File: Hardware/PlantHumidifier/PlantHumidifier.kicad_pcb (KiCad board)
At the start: 2 copper layers, 10 parts, among them J1 110990030, J2 Conn_01x05_Female, J3 Conn_01x04_Female, J4 Conn_01x04_Female, SW1 SW_SPST, U1 WeMos_D1_mini

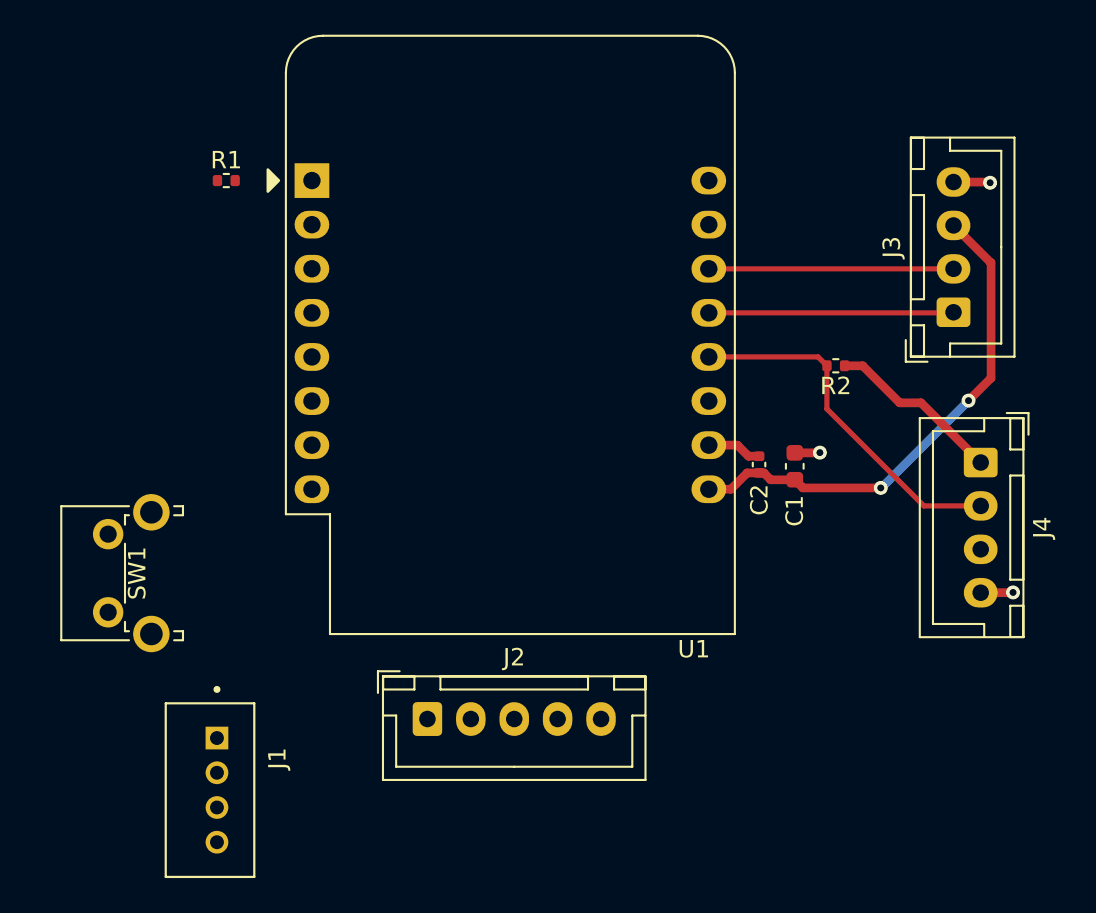
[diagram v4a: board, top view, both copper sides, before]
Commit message: Layout: Reflect new pin changes
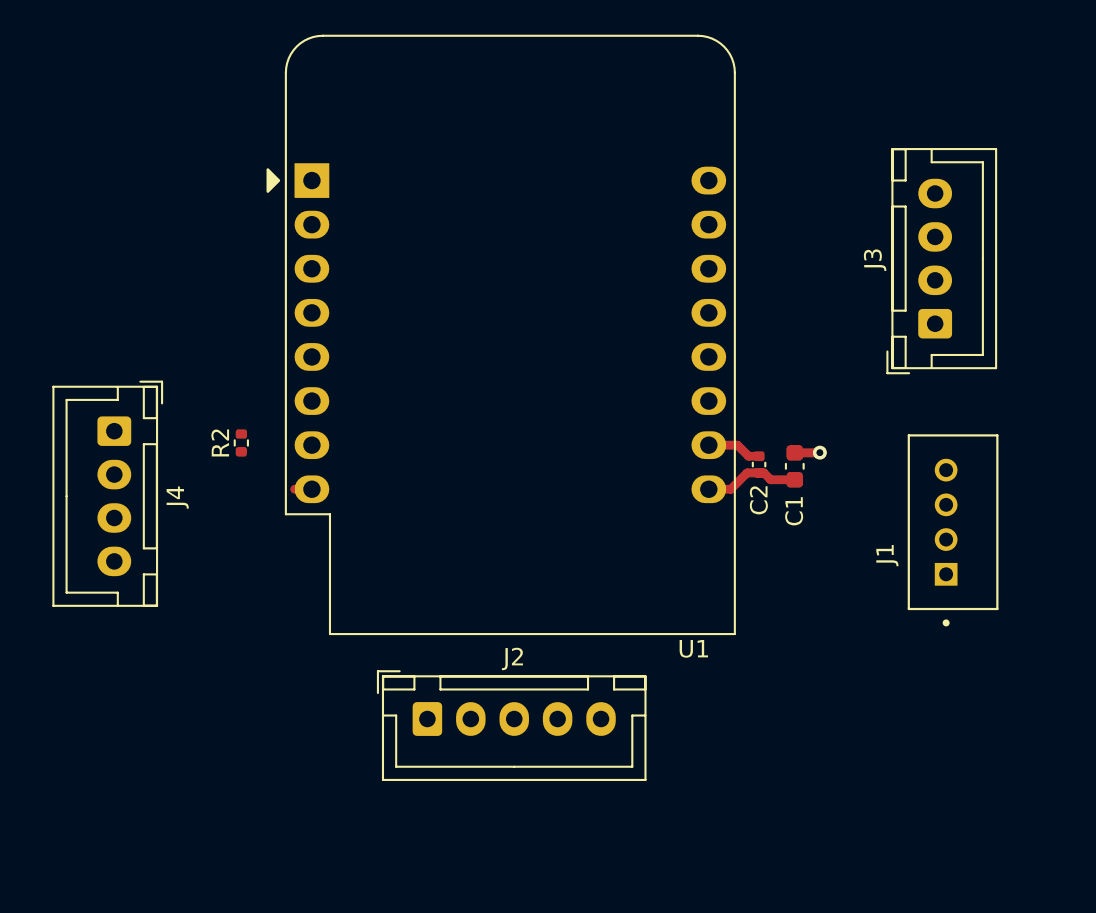
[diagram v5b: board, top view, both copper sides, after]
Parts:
- removed R1: 10k, Resistor_SMD:R_0402_1005Metric
- removed SW1: SW_SPST, Button_Switch_THT:SW_Tactile_SPST_Angled_PTS645Vx83-2LFS
- moved J4 49.9 mm to (66.2, 90.0)
- moved J1 44.7 mm to (114.1, 95.2), turned to 90 degrees
- moved R2 34.5 mm to (73.5, 90.7), turned to 90 degrees
- moved J3 1.25 mm to (113.5, 83.8)
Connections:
- J2 pad 3: /Encoder_SW -> /Rst_n
- J4 pad 1: +3V3 -> /DHT22_Sense
- J4 pad 2: /DHT22_Sense -> +3V3
- U1 pad 12: /DHT22_Sense -> unconnected-(U1-Pad12)
- U1 pad 3: /Encoder_SW -> /Atomizer
- U1 pad 6: unconnected-(U1-Pad6) -> /DHT22_Sense
- U1 pad 7: /Atomizer -> unconnected-(U1-Pad7)
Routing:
- net +5V: track 29.3 -> 5.51 mm, vias 2 -> 0
- net /DHT22_Sense: track 20.7 -> 0.00 mm
- net /OLED_SDA: track 14.1 -> 0.00 mm
- net /OLED_SCL: track 14.1 -> 0.00 mm
- net +3V3: track 10.1 -> 0.99 mm
- net GND: track 8.66 -> 4.66 mm, vias 3 -> 1

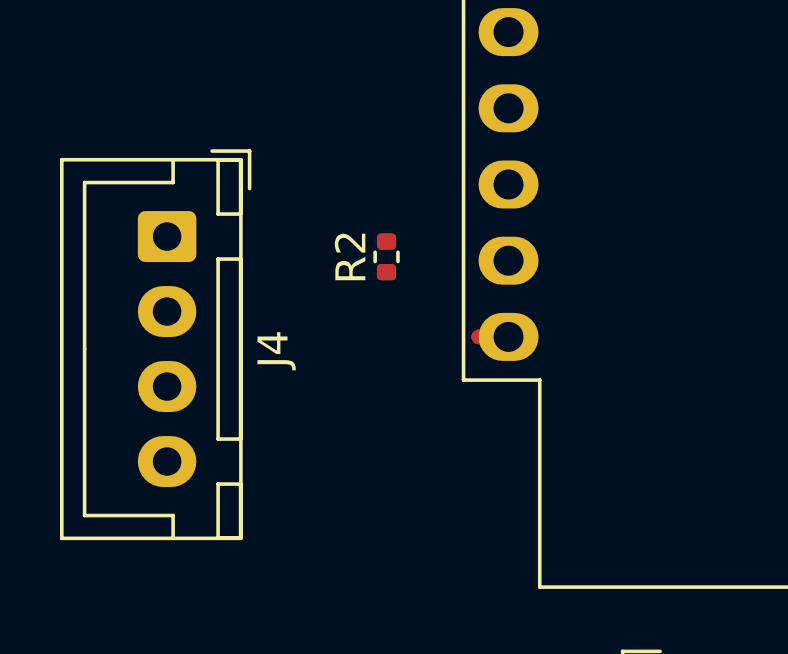
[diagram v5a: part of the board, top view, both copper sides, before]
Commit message: Layout: Route DHT22
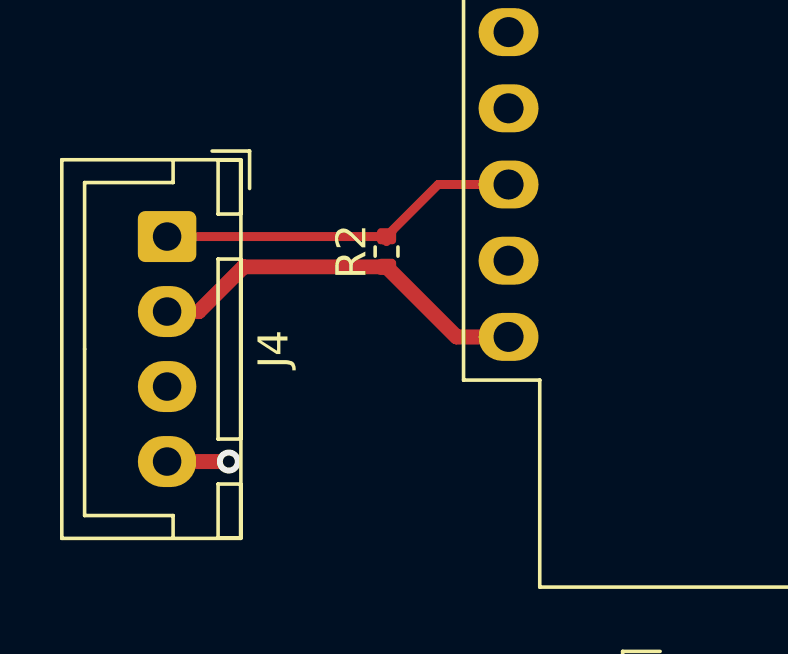
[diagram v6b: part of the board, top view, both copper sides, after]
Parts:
- moved R2 0.18 mm to (73.5, 90.5)
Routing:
- net /DHT22_Sense: track 0.00 -> 12.3 mm
- net +3V3: track 0.99 -> 13.0 mm
- net GND: track 4.66 -> 6.72 mm, vias 1 -> 2
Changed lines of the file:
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@@
   )
   (footprint "Resistor_SMD:R_0402_1005Metric" (layer "F.Cu")
-    (at 73.5076 90.678 90)
+    (at 73.5076 90.5 90)
     (descr "Resistor SMD 0402 (1005 Metric), square (rectangular) end terminal, IPC_7351 nominal, (Body size source: IPC-SM-782 page 72, https://www.pcb-3d.com/wordpress/wp-content/uploads/ipc-sm-782a_amendment_1_and_2.pdf), generated with kicad-footprint-generator")
     (tags "resistor")
@@
   (segment (start 101.7016 93.345) (end 102.644 92.4026) (width 0.5) (layer "F.Cu") (net 1))
   (segment (start 100.434 93.345) (end 101.7016 93.345) (width 0.5) (layer "F.Cu") (net 1))
+  (segment (start 66.1924 97.5) (end 68.25 97.5) (width 0.5) (layer "F.Cu") (net 2))
   (segment (start 106.82 91.2492) (end 106.8324 91.2368) (width 0.5) (layer "F.Cu") (net 2))
   (segment (start 105.3468 91.2114) (end 105.3846 91.2492) (width 0.5) (layer "F.Cu") (net 2))
@@
   (segment (start 102.0826 90.805) (end 102.7202 91.4426) (width 0.5) (layer "F.Cu") (net 2))
   (segment (start 102.7202 91.4426) (end 103.3272 91.4426) (width 0.5) (layer "F.Cu") (net 2))
+  (via (at 68.25 97.5) (size 0.8) (drill 0.4) (layers "F.Cu" "B.Cu") (net 2))
   (via (at 106.8324 91.2368) (size 0.8) (drill 0.4) (layers "F.Cu" "B.Cu") (net 2))
-  (segment (start 77.574 93.345) (end 76.581 93.345) (width 0.5) (layer "F.Cu") (net 10))
+  (segment (start 68.74 91.01) (end 73.5076 91.01) (width 0.5) (layer "F.Cu") (net 10))
+  (segment (start 73.5076 91.01) (end 75.8426 93.345) (width 0.5) (layer "F.Cu") (net 10))
+  (segment (start 75.8426 93.345) (end 77.574 93.345) (width 0.5) (layer "F.Cu") (net 10))
+  (segment (start 67.25 92.5) (end 68.74 91.01) (width 0.5) (layer "F.Cu") (net 10))
+  (segment (start 66.1924 92.5) (end 67.25 92.5) (width 0.5) (layer "F.Cu") (net 10))
+  (segment (start 73.4976 90) (end 73.5076 89.99) (width 0.3) (layer "F.Cu") (net 11))
+  (segment (start 73.5076 89.99) (end 75.2326 88.265) (width 0.3) (layer "F.Cu") (net 11))
+  (segment (start 75.2326 88.265) (end 77.574 88.265) (width 0.3) (layer "F.Cu") (net 11))
+  (segment (start 66.1924 90) (end 73.4976 90) (width 0.3) (layer "F.Cu") (net 11))
+  (segment (start 73.3396 90) (end 73.5076 90.168) (width 0.3) (layer "F.Cu") (net 11))
 )

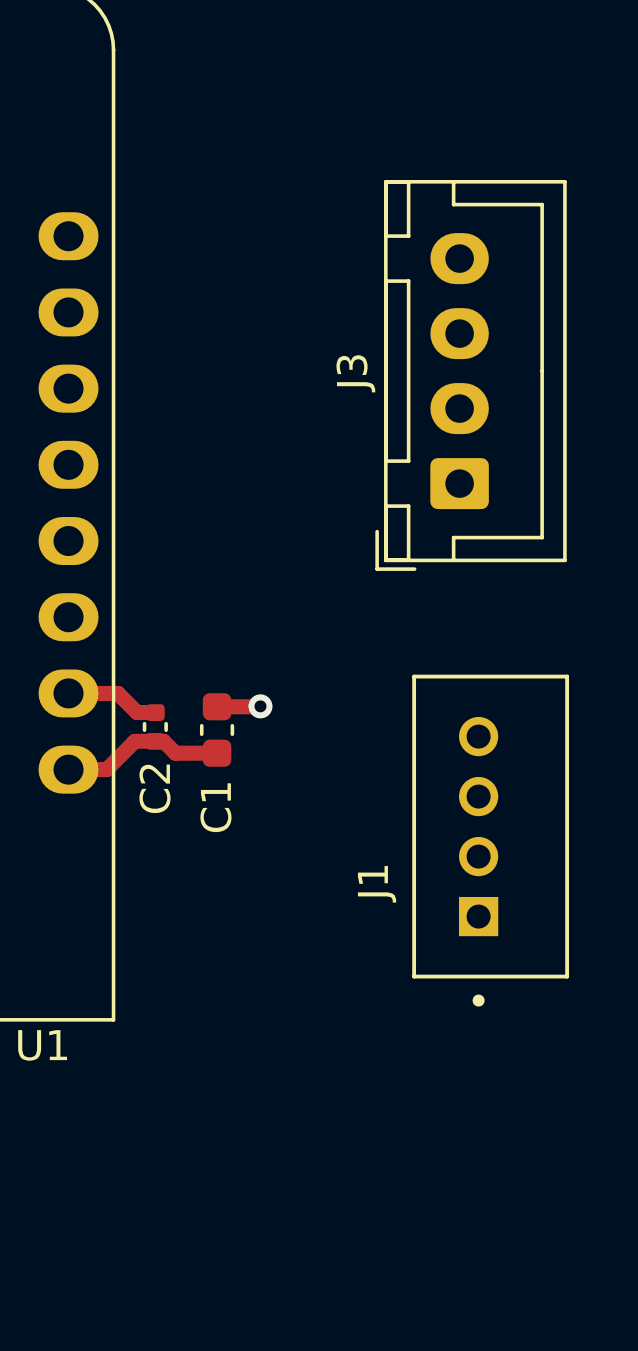
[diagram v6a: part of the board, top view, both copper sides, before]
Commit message: Change pin assignment for OLED for better routing
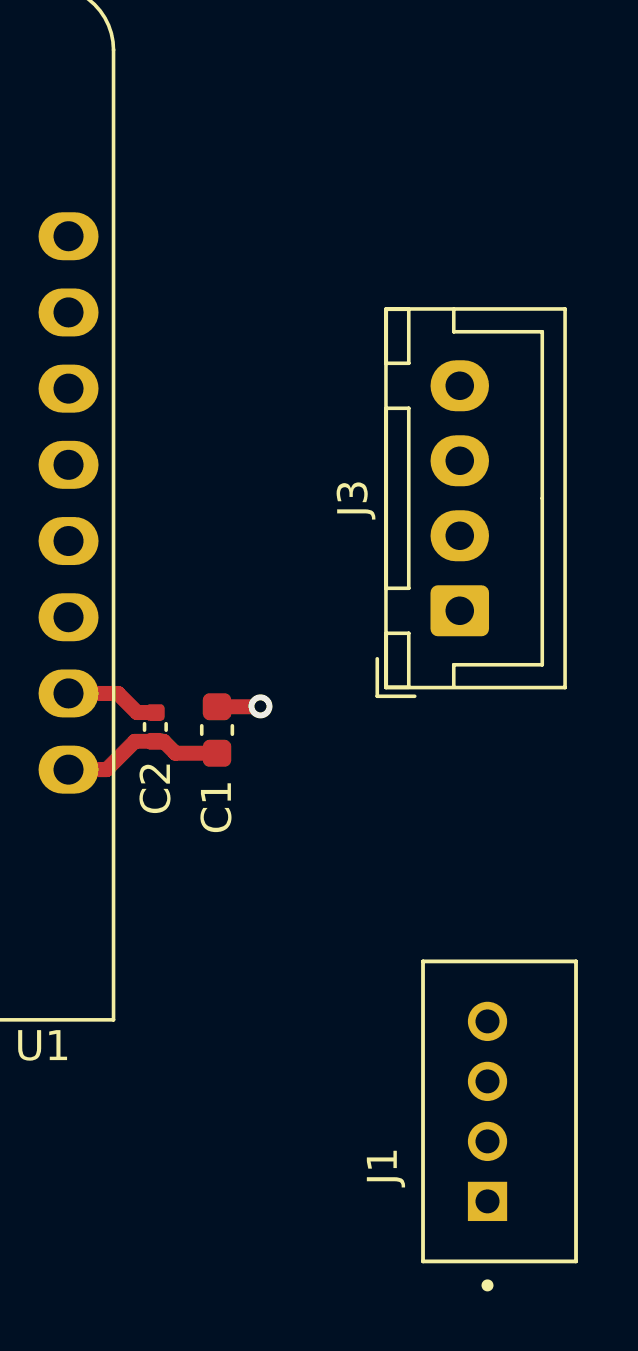
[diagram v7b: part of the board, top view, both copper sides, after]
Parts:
- moved J1 9.50 mm to (114.4, 104.7)
- moved J3 4.24 mm to (113.5, 88.0)
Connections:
- J3 pad 1: /OLED_SDA -> +5V
- J3 pad 2: /OLED_SCL -> GND
- J3 pad 3: +5V -> /OLED_SDA
- J3 pad 4: GND -> /OLED_SCL
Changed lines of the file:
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@@
   )
   (footprint "Connector_JST:JST_XH_B4B-XH-A_1x04_P2.50mm_Vertical" (layer "F.Cu")
-    (at 113.4702 83.8108 90)
+    (at 113.475 88.05 90)
     (descr "JST XH series connector, B4B-XH-A (http://www.jst-mfg.com/product/pdf/eng/eXH.pdf), generated with kicad-footprint-generator")
     (tags "connector JST XH vertical")
@@
     (fp_line (start -2.45 3.4) (end 9.95 3.4) (layer "F.Fab") (width 0.1))
     (pad "1" thru_hole roundrect (at 0 0 90) (size 1.7 1.95) (drill 0.95) (layers *.Cu *.Mask) (roundrect_rratio 0.147059)
-      (net 5 "/OLED_SDA") (pinfunction "Pin_1") (pintype "passive"))
+      (net 1 "+5V") (pinfunction "Pin_1") (pintype "passive"))
     (pad "2" thru_hole oval (at 2.5 0 90) (size 1.7 1.95) (drill 0.95) (layers *.Cu *.Mask)
-      (net 6 "/OLED_SCL") (pinfunction "Pin_2") (pintype "passive"))
+      (net 2 "GND") (pinfunction "Pin_2") (pintype "passive"))
     (pad "3" thru_hole oval (at 5 0 90) (size 1.7 1.95) (drill 0.95) (layers *.Cu *.Mask)
-      (net 1 "+5V") (pinfunction "Pin_3") (pintype "passive"))
+      (net 5 "/OLED_SDA") (pinfunction "Pin_3") (pintype "passive"))
     (pad "4" thru_hole oval (at 7.5 0 90) (size 1.7 1.95) (drill 0.95) (layers *.Cu *.Mask)
-      (net 2 "GND") (pinfunction "Pin_4") (pintype "passive"))
+      (net 6 "/OLED_SCL") (pinfunction "Pin_4") (pintype "passive"))
     (model "${KICAD6_3DMODEL_DIR}/Connector_JST.3dshapes/JST_XH_B4B-XH-A_1x04_P2.50mm_Vertical.wrl"
       (offset (xyz 0 0 0))
@@
   )
   (footprint "Seeed_Connectors:SEEED_110990030" (layer "F.Cu")
-    (at 114.1032 95.2431 90)
+    (at 114.4 104.7375 90)
     (property "MANUFACTURER" "Seeed Technology")
     (property "MAXIMUM_PACKAGE_HEIGHT" "8.1mm")

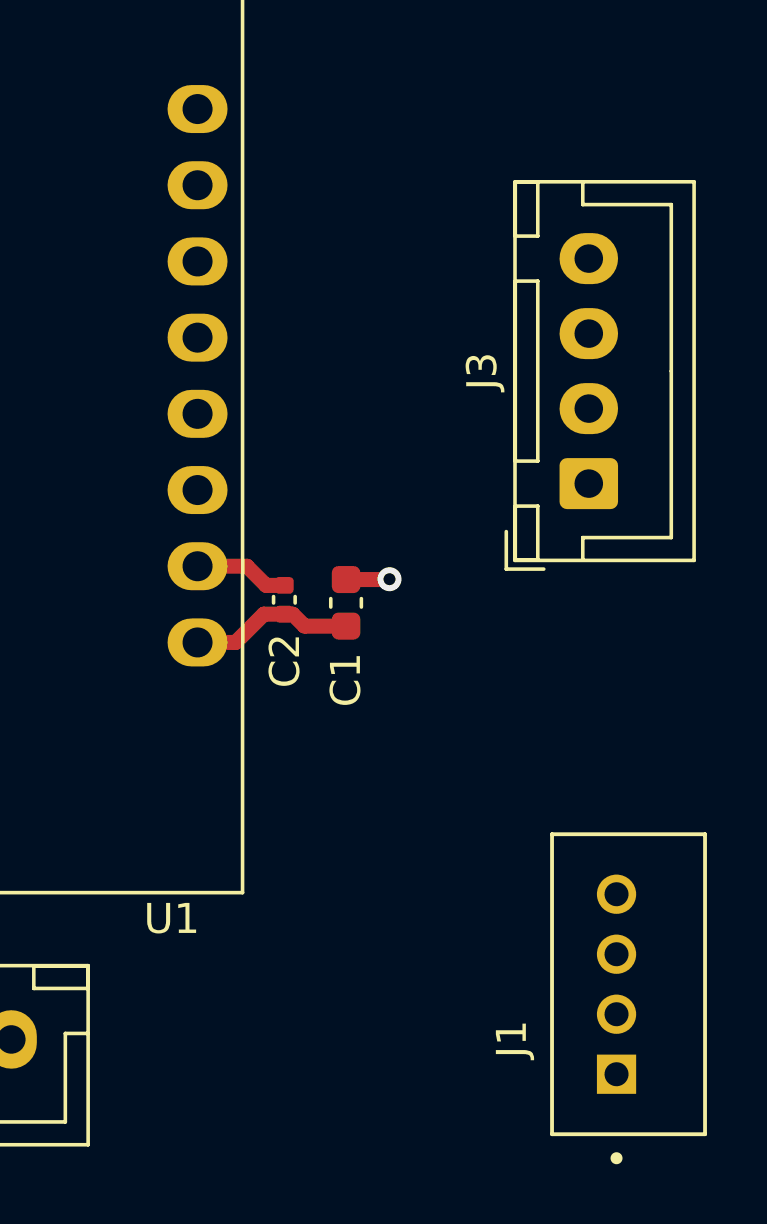
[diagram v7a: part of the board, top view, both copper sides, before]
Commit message: Layout: Route OLED
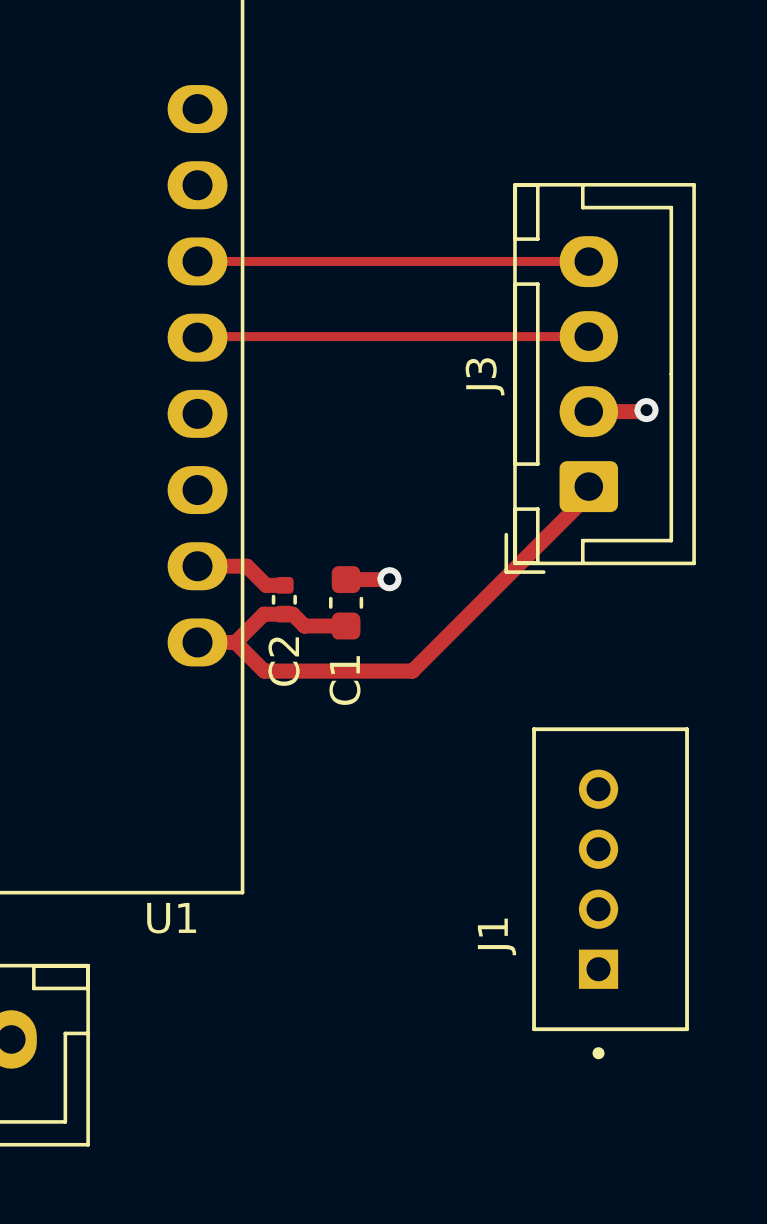
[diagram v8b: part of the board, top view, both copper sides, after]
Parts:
- moved J1 3.55 mm to (113.8, 101.2)
- moved J3 0.10 mm to (113.5, 88.2)
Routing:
- net +5V: track 5.51 -> 20.4 mm
- net /OLED_SDA: track 0.00 -> 13.1 mm
- net /OLED_SCL: track 0.00 -> 13.0 mm
- net GND: track 6.72 -> 8.67 mm, vias 2 -> 3
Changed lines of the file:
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@@
   )
   (footprint "Connector_JST:JST_XH_B4B-XH-A_1x04_P2.50mm_Vertical" (layer "F.Cu")
-    (at 113.475 88.05 90)
+    (at 113.475 88.15 90)
     (descr "JST XH series connector, B4B-XH-A (http://www.jst-mfg.com/product/pdf/eng/eXH.pdf), generated with kicad-footprint-generator")
     (tags "connector JST XH vertical")
@@
   )
   (footprint "Seeed_Connectors:SEEED_110990030" (layer "F.Cu")
-    (at 114.4 104.7375 90)
+    (at 113.8 101.2375 90)
     (property "MANUFACTURER" "Seeed Technology")
     (property "MAXIMUM_PACKAGE_HEIGHT" "8.1mm")
@@
   )
   (segment (start 103.3272 92.4026) (end 103.604 92.4026) (width 0.5) (layer "F.Cu") (net 1))
+  (segment (start 113.475 88.425) (end 107.6 94.3) (width 0.5) (layer "F.Cu") (net 1))
+  (segment (start 102.6566 94.3) (end 101.7016 93.345) (width 0.5) (layer "F.Cu") (net 1))
+  (segment (start 107.6 94.3) (end 102.6566 94.3) (width 0.5) (layer "F.Cu") (net 1))
   (segment (start 104.0006 92.7992) (end 105.3846 92.7992) (width 0.5) (layer "F.Cu") (net 1))
   (segment (start 103.604 92.4026) (end 104.0006 92.7992) (width 0.5) (layer "F.Cu") (net 1))
   (segment (start 102.644 92.4026) (end 103.3272 92.4026) (width 0.5) (layer "F.Cu") (net 1))
+  (segment (start 113.475 88.15) (end 113.475 88.425) (width 0.5) (layer "F.Cu") (net 1))
   (segment (start 101.7016 93.345) (end 102.644 92.4026) (width 0.5) (layer "F.Cu") (net 1))
   (segment (start 100.434 93.345) (end 101.7016 93.345) (width 0.5) (layer "F.Cu") (net 1))
@@
   (segment (start 100.434 90.805) (end 102.0826 90.805) (width 0.5) (layer "F.Cu") (net 2))
   (segment (start 105.3846 91.2492) (end 106.82 91.2492) (width 0.5) (layer "F.Cu") (net 2))
+  (segment (start 113.475 85.65) (end 115.35 85.65) (width 0.5) (layer "F.Cu") (net 2))
   (segment (start 102.0826 90.805) (end 102.7202 91.4426) (width 0.5) (layer "F.Cu") (net 2))
   (segment (start 102.7202 91.4426) (end 103.3272 91.4426) (width 0.5) (layer "F.Cu") (net 2))
+  (segment (start 115.35 85.65) (end 115.4 85.6) (width 0.5) (layer "F.Cu") (net 2))
   (via (at 68.25 97.5) (size 0.8) (drill 0.4) (layers "F.Cu" "B.Cu") (net 2))
   (via (at 106.8324 91.2368) (size 0.8) (drill 0.4) (layers "F.Cu" "B.Cu") (net 2))
+  (via (at 115.4 85.6) (size 0.8) (drill 0.4) (layers "F.Cu" "B.Cu") (net 2))
+  (segment (start 100.469 83.15) (end 100.434 83.185) (width 0.3) (layer "F.Cu") (net 5))
+  (segment (start 113.475 83.15) (end 100.469 83.15) (width 0.3) (layer "F.Cu") (net 5))
+  (segment (start 113.47 80.645) (end 113.475 80.65) (width 0.3) (layer "F.Cu") (net 6))
+  (segment (start 100.434 80.645) (end 113.47 80.645) (width 0.3) (layer "F.Cu") (net 6))
   (segment (start 68.74 91.01) (end 73.5076 91.01) (width 0.5) (layer "F.Cu") (net 10))
   (segment (start 73.5076 91.01) (end 75.8426 93.345) (width 0.5) (layer "F.Cu") (net 10))
